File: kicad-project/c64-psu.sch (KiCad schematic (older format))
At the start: 40 parts, among them J1 Conn_01x02, J2 Conn_01x02, J3 Conn_01x02, Q1 N-MOS, U1 MAX6399, U2 LMR33630A

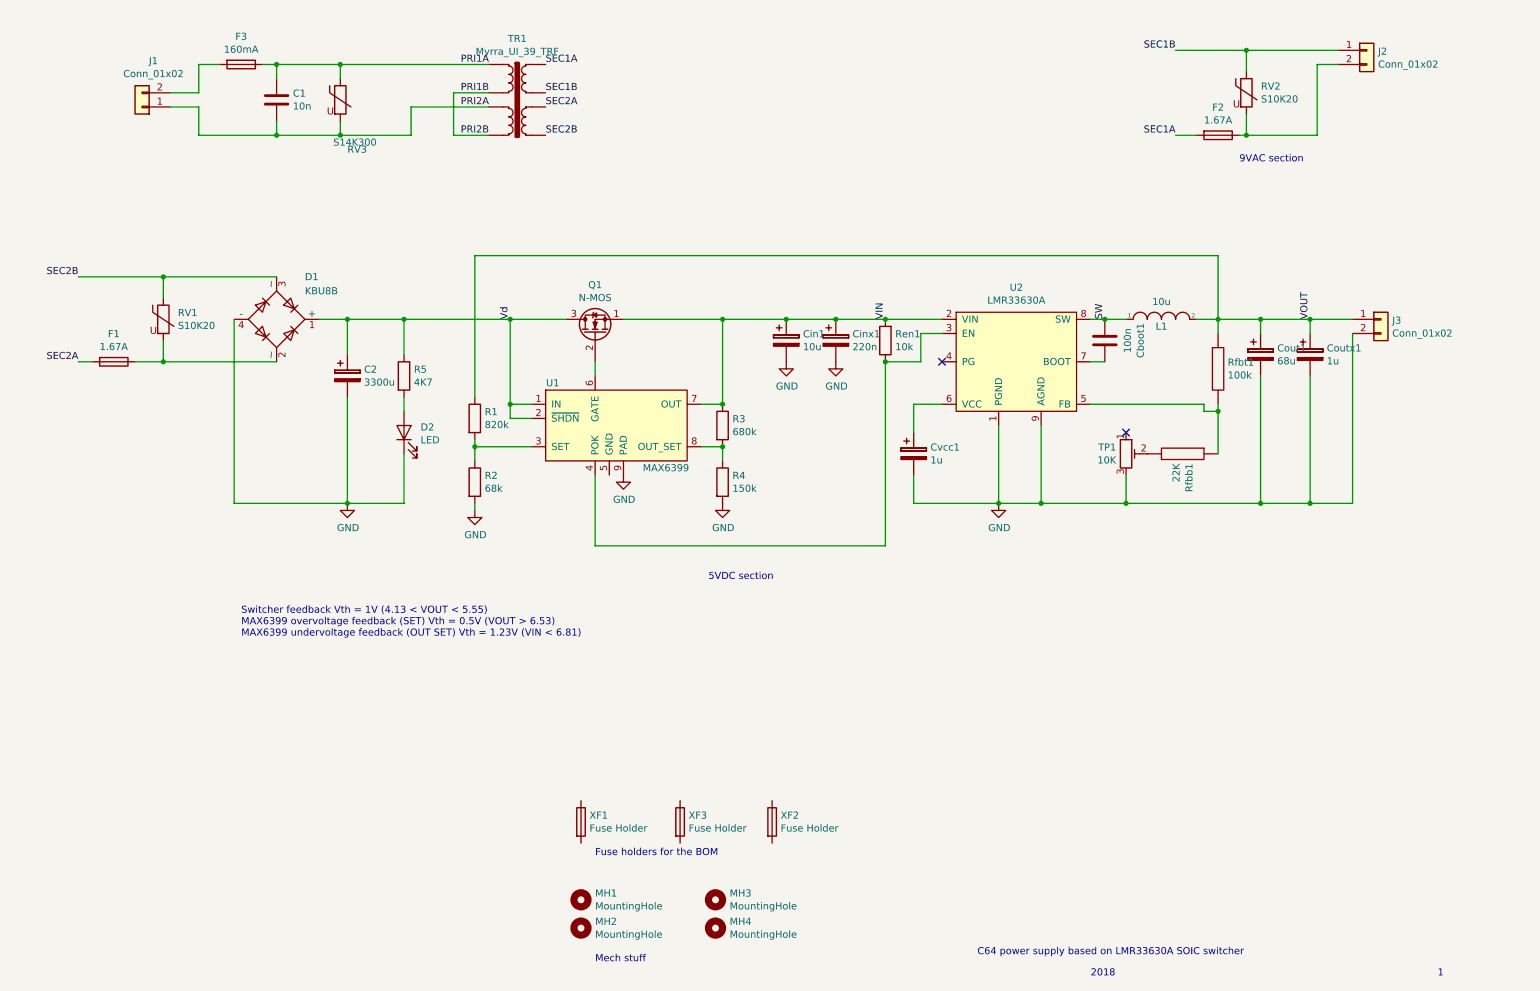
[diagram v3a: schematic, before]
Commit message: HF noise improvements (reduce high di/dt loop area, reduce SW node area, etc.).
Also:

+ Moved trf's origin to pin 1
+ Replaced 5 mm pitch connectors with (apparently safer) 7.62 mm

ToDo:

- Could be further improved by fitting the switcher between the filter cap legs on the bottom side! Will try that next.
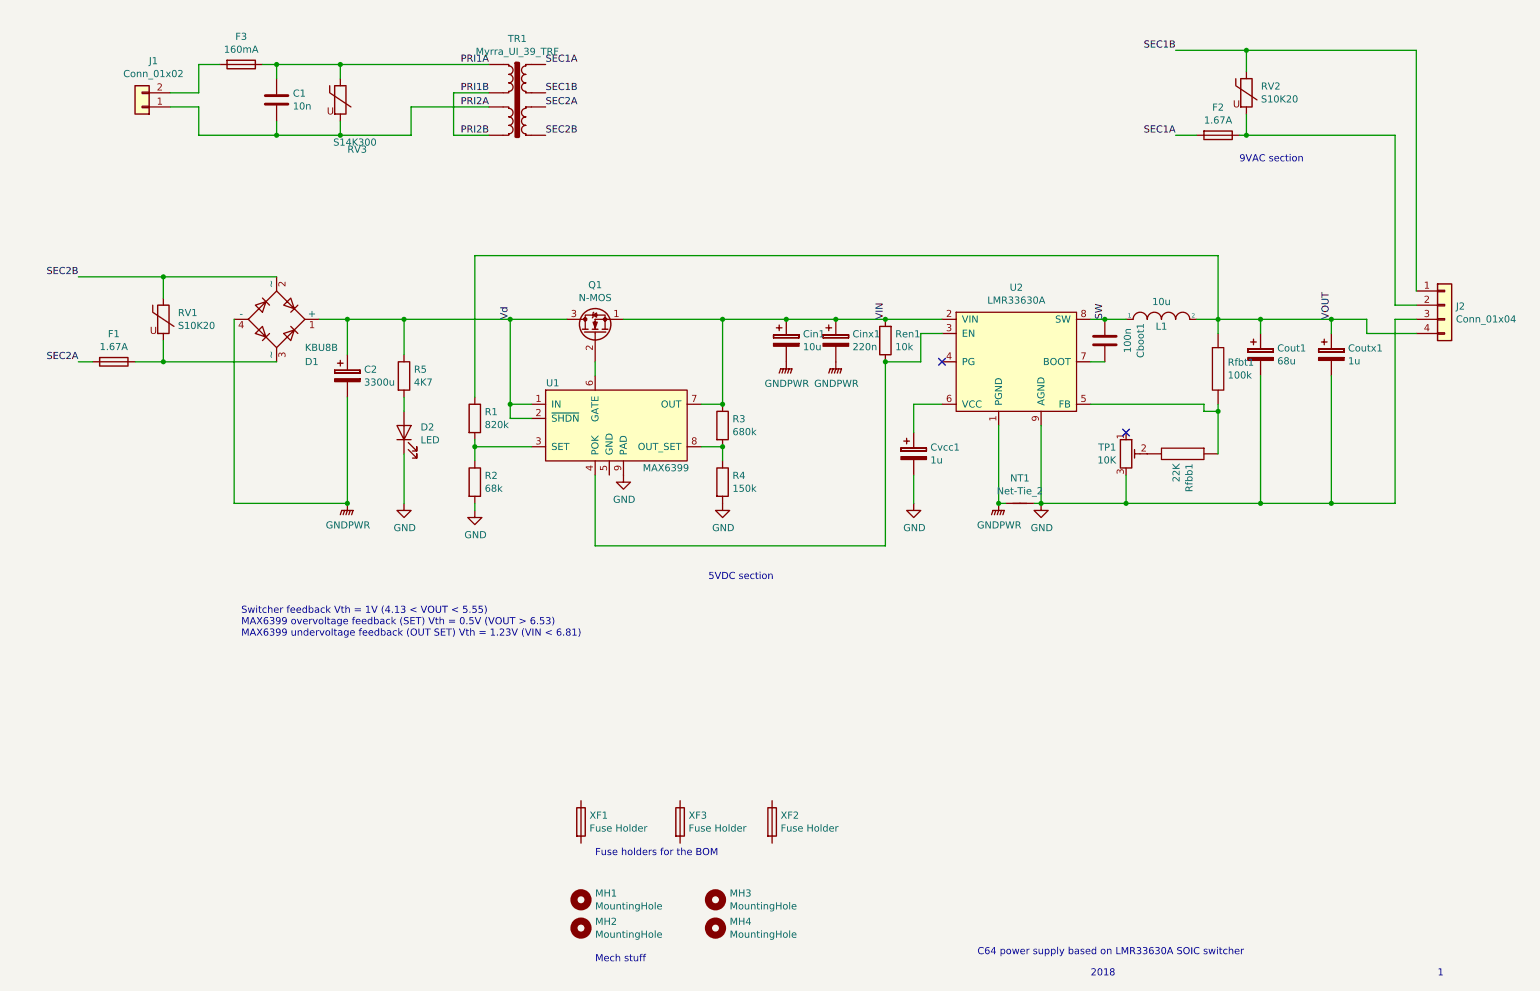
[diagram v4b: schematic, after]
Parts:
- removed J2, J3: Conn_01x02, TerminalBlock_Phoenix:TerminalBlock_Phoenix_MKDS-1,5-2_1x02_P5.00mm_Horizontal, symbol Connector_Generic:Conn_01x02
- added J2: Conn_01x04, c64-psu:KF7.62_4P, symbol Connector_Generic:Conn_01x04
- added NT1: Net-Tie_2, NetTie:NetTie-2_THT_Pad1.0mm, symbol Device:Net-Tie_2
- J1: footprint TerminalBlock_Phoenix:TerminalBlock_Phoenix_MKDS-1,5-2_1x02_P5.00mm_Horizontal -> c64-psu:KF7.62_2P
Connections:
- net GND: now also J2.3 (Pin_3), NT1.2; no longer C2.2, Cin1.2, Cinx1.2, D1.4 (-), U2.1 (PGND)
- net SEC1B: now also J2.1 (Pin_1)
- net SEC2B: now also D1.2 (~~); no longer D1.3 (~~)
- net VOUT: now also J2.4 (Pin_4)
- net at F1.1, RV1.2: now also D1.3 (~~); no longer D1.2 (~~)
- net at F2.1, RV2.2: now also J2.2 (Pin_2)
- new net GNDPWR: C2.2, Cin1.2, Cinx1.2, D1.4 (-), NT1.1, U2.1 (PGND)
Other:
- moved on the sheet: Coutx1
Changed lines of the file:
@@
 F 6 "905-KBU8B" H 0   0   50  0001 C CNN "MouserCode"
 	1    2400 3000
-	1    0    0    -1
+	1    0    0    1
 $EndComp
 Wire Wire Line
@@
 L Device:CP Coutx1
 U 1 1 5BB130FD
-P 9700 3250
-F 0 "Coutx1" H 9818 3296 50  0000 L CNN
-F 1 "1u" H 9818 3205 50  0000 L CNN
-F 2 "Capacitor_SMD:C_0805_2012Metric_Pad1.15x1.40mm_HandSolder" H 9738 3100 50  0001 C CNN
-F 3 "" H 9700 3250 50  0001 C CNN
-F 4 "GRM21BR71A105KA01L" H 150 100 50  0001 C CNN "MfrCode"
-F 5 "Murata" H 0   0   50  0001 C CNN "Mfr"
-F 6 "81-GRM40X105K10L" H 0   0   50  0001 C CNN "MouserCode"
-	1    9700 3250
-	1    0    0    -1
-$EndComp
-$Comp
-L power:GND #PWR01
-U 1 1 5BB13412
-P 2900 4300
-F 0 "#PWR01" H 2900 4050 50  0001 C CNN
-F 1 "GND" H 2905 4127 50  0000 C CNN
-F 2 "" H 2900 4300 50  0001 C CNN
-F 3 "" H 2900 4300 50  0001 C CNN
-	1    2900 4300
+P 9850 3250
+F 0 "Coutx1" H 9968 3296 50  0000 L CNN
+F 1 "1u" H 9968 3205 50  0000 L CNN
+F 2 "Capacitor_SMD:C_0805_2012Metric_Pad1.15x1.40mm_HandSolder" H 9888 3100 50  0001 C CNN
+F 3 "" H 9850 3250 50  0001 C CNN
+F 4 "GRM21BR71A105KA01L" H 300 100 50  0001 C CNN "MfrCode"
+F 5 "Murata" H 150 0   50  0001 C CNN "Mfr"
+F 6 "81-GRM40X105K10L" H 150 0   50  0001 C CNN "MouserCode"
+	1    9850 3250
 	1    0    0    -1
 $EndComp
@@
 Connection ~ 9050 3000
 Wire Wire Line
-	9700 3000 9700 3100
+	9850 3000 9850 3100
 Connection ~ 9350 3000
 Wire Wire Line
 	9350 3400 9350 4300
-Connection ~ 9350 4300
-Wire Wire Line
-	9700 3400 9700 4300
+Wire Wire Line
+	9850 3400 9850 4300
 Wire Wire Line
 	9050 3600 9050 3650
@@
 	8950 3650 9050 3650
 Connection ~ 9050 3650
-Wire Wire Line
-	7500 3750 7500 4300
-Connection ~ 7500 4300
 Wire Wire Line
 	7800 3750 7800 4300
@@
 Wire Wire Line
 	6900 4100 6900 4300
-Wire Wire Line
-	6900 4300 7500 4300
 $Comp
 L Device:CP Cin1
@@
 	1    0    0    -1
 $EndComp
-$Comp
-L Connector_Generic:Conn_01x02 J3
-U 1 1 5BB1E923
-P 10200 3000
-F 0 "J3" H 10280 2992 50  0000 L CNN
-F 1 "Conn_01x02" H 10280 2901 50  0000 L CNN
-F 2 "TerminalBlock_Phoenix:TerminalBlock_Phoenix_MKDS-1,5-2_1x02_P5.00mm_Horizontal" H 10200 3000 50  0001 C CNN
-F 3 "" H 10200 3000 50  0001 C CNN
-F 4 "Any" H 0   -100 50  0001 C CNN "Mfr"
-F 5 "Aliexpress: 'KF301-5.0-2P'" H 0   -100 50  0001 C CNN "MfrCode"
-	1    10200 3000
-	1    0    0    -1
-$EndComp
-$Comp
-L Connector_Generic:Conn_01x02 J2
-U 1 1 5BB20295
-P 10100 1100
-F 0 "J2" H 10180 1092 50  0000 L CNN
-F 1 "Conn_01x02" H 10180 1001 50  0000 L CNN
-F 2 "TerminalBlock_Phoenix:TerminalBlock_Phoenix_MKDS-1,5-2_1x02_P5.00mm_Horizontal" H 10100 1100 50  0001 C CNN
-F 3 "" H 10100 1100 50  0001 C CNN
-F 4 "Any" H 7250 -3800 50  0001 C CNN "Mfr"
-F 5 "Aliexpress: 'KF301-5.0-2P'" H 7250 -3800 50  0001 C CNN "MfrCode"
-	1    10100 1100
-	1    0    0    -1
-$EndComp
 Wire Wire Line
 	8750 1100 9250 1100
-Wire Wire Line
-	9250 1100 9900 1100
 Text Notes 7350 7500 0    50   ~ 0
 C64 power supply based on LMR33630A SOIC switcher
@@
 F 0 "J1" H 1370 1175 50  0000 C CNN
 F 1 "Conn_01x02" H 1370 1266 50  0000 C CNN
-F 2 "TerminalBlock_Phoenix:TerminalBlock_Phoenix_MKDS-1,5-2_1x02_P5.00mm_Horizontal" H 1450 1500 50  0001 C CNN
+F 2 "c64-psu:KF7.62_2P" H 1450 1500 50  0001 C CNN
 F 3 "" H 1450 1500 50  0001 C CNN
 F 4 "Any" H 0   0   50  0001 C CNN "Mfr"
@@
 Wire Wire Line
 	9200 1700 9250 1700
-Wire Wire Line
-	9750 1700 9750 1200
-Wire Wire Line
-	9750 1200 9900 1200
 $Comp
 L Device:Varistor RV1
@@
 Wire Wire Line
 	9250 1100 9250 1250
-Connection ~ 9250 1100
 Wire Wire Line
 	9250 1550 9250 1700
 Connection ~ 9250 1700
 Wire Wire Line
-	9250 1700 9750 1700
+	9250 1700 10300 1700
 $Comp
 L Device:R_POT_TRIM TP1
@@
 Wire Wire Line
 	8400 4100 8400 4300
-Connection ~ 8400 4300
-Wire Wire Line
-	8400 4300 9350 4300
 Wire Wire Line
 	9050 3650 9050 3950
@@
 Wire Wire Line
 	7800 4300 8400 4300
-Wire Wire Line
-	7500 4300 7800 4300
 $Comp
 L Device:R R1
@@
 Wire Wire Line
 	3800 4300 3800 4350
-Connection ~ 9700 3000
-Connection ~ 9700 4300
 Wire Wire Line
 	1000 2700 1600 2700
@@
 Text Label 6700 3000 1    50   ~ 0
 VIN
-Text Label 9700 3000 1    50   ~ 0
+Text Label 9850 3000 1    50   ~ 0
 VOUT
 $Comp
@@
 L power:GND #PWR07
 U 1 1 5BD4DE67
-P 7500 4300
-F 0 "#PWR07" H 7500 4050 50  0001 C CNN
-F 1 "GND" H 7505 4127 50  0000 C CNN
-F 2 "" H 7500 4300 50  0001 C CNN
-F 3 "" H 7500 4300 50  0001 C CNN
-	1    7500 4300
+P 7800 4300
+F 0 "#PWR07" H 7800 4050 50  0001 C CNN
+F 1 "GND" H 7805 4127 50  0000 C CNN
+F 2 "" H 7800 4300 50  0001 C CNN
+F 3 "" H 7800 4300 50  0001 C CNN
+	1    7800 4300
 	1    0    0    -1
 $EndComp
@@
 Wire Wire Line
 	8250 3000 8400 3000
-Wire Wire Line
-	9700 3000 10000 3000
-Wire Wire Line
-	9700 4300 10000 4300
 $Comp
 L Device:R R4
@@
 	2900 3000 3300 3000
 Wire Wire Line
-	9350 4300 9700 4300
+	9350 4300 9850 4300
 Connection ~ 6000 3000
 Connection ~ 6350 3000
@@
 	4650 4600 6700 4600
 Connection ~ 6700 3300
-$Comp
-L power:GND #PWR05
-U 1 1 5BDE946A
-P 6000 3300
-F 0 "#PWR05" H 6000 3050 50  0001 C CNN
-F 1 "GND" H 6005 3127 50  0000 C CNN
-F 2 "" H 6000 3300 50  0001 C CNN
-F 3 "" H 6000 3300 50  0001 C CNN
-	1    6000 3300
-	1    0    0    -1
-$EndComp
-$Comp
-L power:GND #PWR06
-U 1 1 5BDE94B5
-P 6350 3300
-F 0 "#PWR06" H 6350 3050 50  0001 C CNN
-F 1 "GND" H 6355 3127 50  0000 C CNN
-F 2 "" H 6350 3300 50  0001 C CNN
-F 3 "" H 6350 3300 50  0001 C CNN
-	1    6350 3300
-	1    0    0    -1
-$EndComp
 $Comp
 L Device:R R5
@@
 	1    0    0    -1
 $EndComp
-Wire Wire Line
-	2900 4300 3300 4300
 Wire Wire Line
 	3300 3250 3300 3000
@@
 $EndComp
 Wire Wire Line
-	9350 3000 9700 3000
+	9350 3000 9850 3000
 $Comp
 L Device:Fuse XF1
@@
 Wire Wire Line
 	3650 1700 3900 1700
-Wire Wire Line
-	10000 3100 10000 4300
 Text Notes 2150 5250 0    50   ~ 0
 Switcher feedback Vth = 1V (4.13 < VOUT < 5.55)\nMAX6399 overvoltage feedback (SET) Vth = 0.5V (VOUT > 6.53)\nMAX6399 undervoltage feedback (OUT SET) Vth = 1.23V (VIN < 6.81)
+$Comp
+L power:GNDPWR #PWR0101
+U 1 1 5C1FF3CA
+P 7500 4300
+F 0 "#PWR0101" H 7500 4100 50  0001 C CNN
+F 1 "GNDPWR" H 7504 4146 50  0000 C CNN
+F 2 "" H 7500 4250 50  0001 C CNN
+F 3 "" H 7500 4250 50  0001 C CNN
+	1    7500 4300
+	1    0    0    -1
+$EndComp
+$Comp
+L Device:Net-Tie_2 NT1
+U 1 1 5C1FFDC4
+P 7650 4300
+F 0 "NT1" H 7650 4478 50  0000 C CNN
+F 1 "Net-Tie_2" H 7650 4387 50  0000 C CNN
+F 2 "NetTie:NetTie-2_THT_Pad1.0mm" H 7650 4300 50  0001 C CNN
+F 3 "~" H 7650 4300 50  0001 C CNN
+	1    7650 4300
+	1    0    0    -1
+$EndComp
+Wire Wire Line
+	7500 3750 7500 4300
+$Comp
+L power:GND #PWR0102
+U 1 1 5C209985
+P 6900 4300
+F 0 "#PWR0102" H 6900 4050 50  0001 C CNN
+F 1 "GND" H 6905 4127 50  0000 C CNN
+F 2 "" H 6900 4300 50  0001 C CNN
+F 3 "" H 6900 4300 50  0001 C CNN
+	1    6900 4300
+	1    0    0    -1
+$EndComp
+Wire Wire Line
+	7550 4300 7500 4300
+Connection ~ 7500 4300
+Wire Wire Line
+	7750 4300 7800 4300
+$Comp
+L power:GNDPWR #PWR0103
+U 1 1 5C214F36
+P 2900 4300
+F 0 "#PWR0103" H 2900 4100 50  0001 C CNN
+F 1 "GNDPWR" H 2904 4146 50  0000 C CNN
+F 2 "" H 2900 4250 50  0001 C CNN
+F 3 "" H 2900 4250 50  0001 C CNN
+	1    2900 4300
+	1    0    0    -1
+$EndComp
+Connection ~ 9350 4300
+Connection ~ 8400 4300
+Wire Wire Line
+	8400 4300 9350 4300
+$Comp
+L power:GNDPWR #PWR0104
+U 1 1 5C216998
+P 6000 3300
+F 0 "#PWR0104" H 6000 3100 50  0001 C CNN
+F 1 "GNDPWR" H 6004 3146 50  0000 C CNN
+F 2 "" H 6000 3250 50  0001 C CNN
+F 3 "" H 6000 3250 50  0001 C CNN
+	1    6000 3300
+	1    0    0    -1
+$EndComp
+$Comp
+L power:GNDPWR #PWR0105
+U 1 1 5C2171CE
+P 6350 3300
+F 0 "#PWR0105" H 6350 3100 50  0001 C CNN
+F 1 "GNDPWR" H 6354 3146 50  0000 C CNN
+F 2 "" H 6350 3250 50  0001 C CNN
+F 3 "" H 6350 3250 50  0001 C CNN
+	1    6350 3300
+	1    0    0    -1
+$EndComp
+$Comp
+L power:GND #PWR0106
+U 1 1 5C218F35
+P 3300 4300
+F 0 "#PWR0106" H 3300 4050 50  0001 C CNN
+F 1 "GND" H 3305 4127 50  0000 C CNN
+F 2 "" H 3300 4300 50  0001 C CNN
+F 3 "" H 3300 4300 50  0001 C CNN
+	1    3300 4300
+	1    0    0    -1
+$EndComp
+$Comp
+L Connector_Generic:Conn_01x04 J2
+U 1 1 5C21D271
+P 10650 2900
+F 0 "J2" H 10730 2892 50  0000 L CNN
+F 1 "Conn_01x04" H 10730 2801 50  0000 L CNN
+F 2 "c64-psu:KF7.62_4P" H 10650 2900 50  0001 C CNN
+F 3 "~" H 10650 2900 50  0001 C CNN
+	1    10650 2900
+	1    0    0    -1
+$EndComp
+Wire Wire Line
+	10300 1700 10300 2900
+Wire Wire Line
+	10300 2900 10450 2900
+Wire Wire Line
+	9250 1100 10450 1100
+Wire Wire Line
+	10450 1100 10450 2800
+Connection ~ 9250 1100
+Wire Wire Line
+	9850 4300 10300 4300
+Wire Wire Line
+	10300 4300 10300 3000
+Wire Wire Line
+	10300 3000 10450 3000
+Connection ~ 9850 4300
+Wire Wire Line
+	10450 3100 10100 3100
+Wire Wire Line
+	10100 3100 10100 3000
+Wire Wire Line
+	10100 3000 9850 3000
+Connection ~ 9850 3000
 $EndSCHEMATC

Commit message: v2018.2 ready for mfr
+ replaced terminal blocks with quick-disconnect / spade connectors +
+ added footprints for fuses
+ enclosure redone in fusion 3d (sorry freecad 0.17 bodies are not mature yet, I tried)
+ gerbers ready for prod
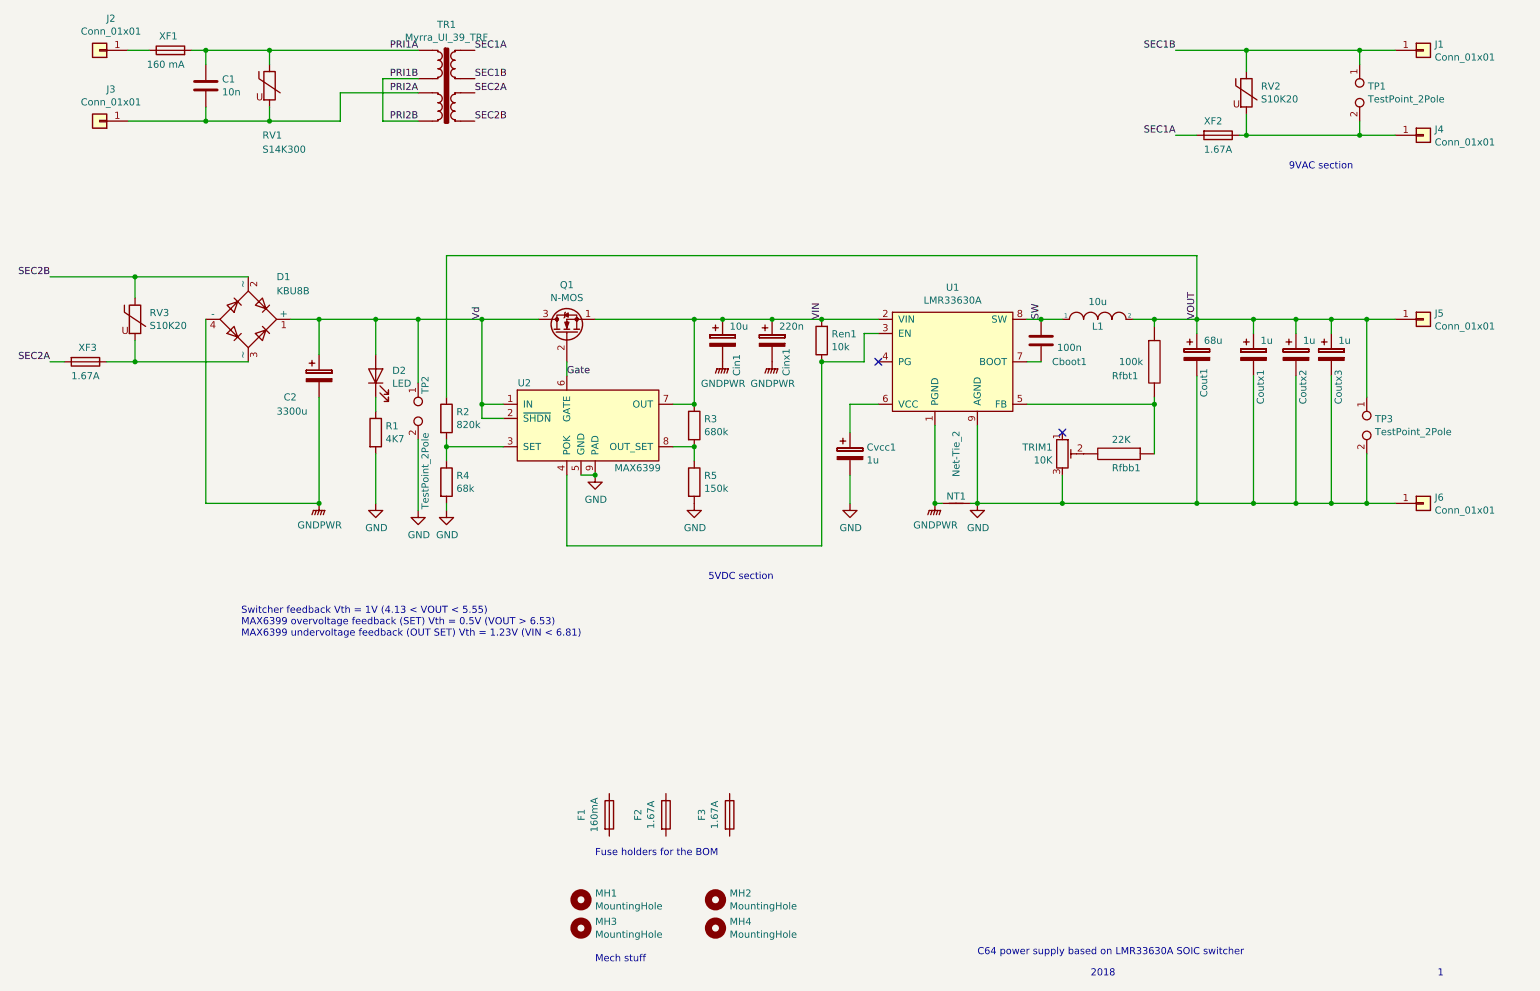
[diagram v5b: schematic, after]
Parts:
- removed J1: Conn_01x02, c64-psu:KF7.62_2P, symbol Connector_Generic:Conn_01x02
- removed J2: Conn_01x04, c64-psu:KF7.62_4P, symbol Connector_Generic:Conn_01x04
- added Coutx1, Coutx2: 1u, Capacitor_SMD:C_0805_2012Metric_Pad1.15x1.40mm_HandSolder, symbol Device:CP
- added J1, J2, J3, J4, J5, J6: Conn_01x01, c64-psu:spade_4.8mm, symbol Connector_Generic:Conn_01x01
- added TP1, TP2, TP3: TestPoint_2Pole, TestPoint:TestPoint_2Pads_Pitch2.54mm_Drill0.8mm, symbol Connector:TestPoint_2Pole
- F1: renamed from F3; footprint Fuse:Fuseholder_Cylinder-5x20mm_Schurter_0031_8201_Horizontal_Open -> c64-psu:20mm fuse
- F2: renamed from F1; footprint Fuse:Fuseholder_Cylinder-5x20mm_Schurter_0031_8201_Horizontal_Open -> c64-psu:20mm fuse
- F3: renamed from F2; footprint Fuse:Fuseholder_Cylinder-5x20mm_Schurter_0031_8201_Horizontal_Open -> c64-psu:20mm fuse
- XF1: renamed from XF3; value Fuse Holder -> 160 mA; footprint (none) -> Fuse:Fuseholder_Cylinder-5x20mm_Schurter_0031_8201_Horizontal_Open
- XF2: value Fuse Holder -> 1.67A; footprint (none) -> Fuse:Fuseholder_Cylinder-5x20mm_Schurter_0031_8201_Horizontal_Open
- XF3: renamed from XF1; value Fuse Holder -> 1.67A; footprint (none) -> Fuse:Fuseholder_Cylinder-5x20mm_Schurter_0031_8201_Horizontal_Open
- renumbered Coutx1 to Coutx3, MH3 to MH2, MH2 to MH3, R5 to R1, R1 to R2, R2 to R4, R4 to R5, RV3 to RV1, RV1 to RV3, TP1 to TRIM1, U2 to U1, U1 to U2
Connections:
- net GND: now also R1.2, U2.5 (GND), Coutx1.2, Coutx2.2, J6.1 (Pin_1), TP2.2, TP3.2; no longer D2.1 (K)
- net PRI1A: now also XF1.2; no longer F1.1
- net PRI2A: now also J3.1 (Pin_1)
- net SEC1A: now also XF2.2; no longer F3.2
- net SEC1B: now also J1.1 (Pin_1), TP1.1
- net SEC2A: now also XF3.2; no longer F2.2
- net VOUT: now also Coutx1.1, Coutx2.1, J5.1 (Pin_1), TP3.1
- net Vd: now also D2.2 (A), TP2.1; no longer R1.1
- net at D1.3 (~~), RV3.2: now also XF3.1; no longer F2.1
- net at F3.1: no longer RV2.2
- net Gate: now reaches Q1.2 (G), U2.6 (GATE)
- net at XF2.1: now also RV2.2, J4.1 (Pin_1), TP1.2
- net at XF1.1: now also J2.1 (Pin_1)
- new net: D2.1 (K), R1.1
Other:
- moved on the sheet: C1, C2, Cboot1, Cin1, Cinx1, Cout1, Cvcc1, D1, D2, F1, F2, F3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
